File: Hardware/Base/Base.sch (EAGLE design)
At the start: 69 parts, among them T1 2N3904, T10 2N3904, T11 2N3904, T2 2N3904, T3 2N3904, T4 2N3904, T5 2N3904, T6 2N3904, T7 2N3904, T8 2N3904, T9 2N3904

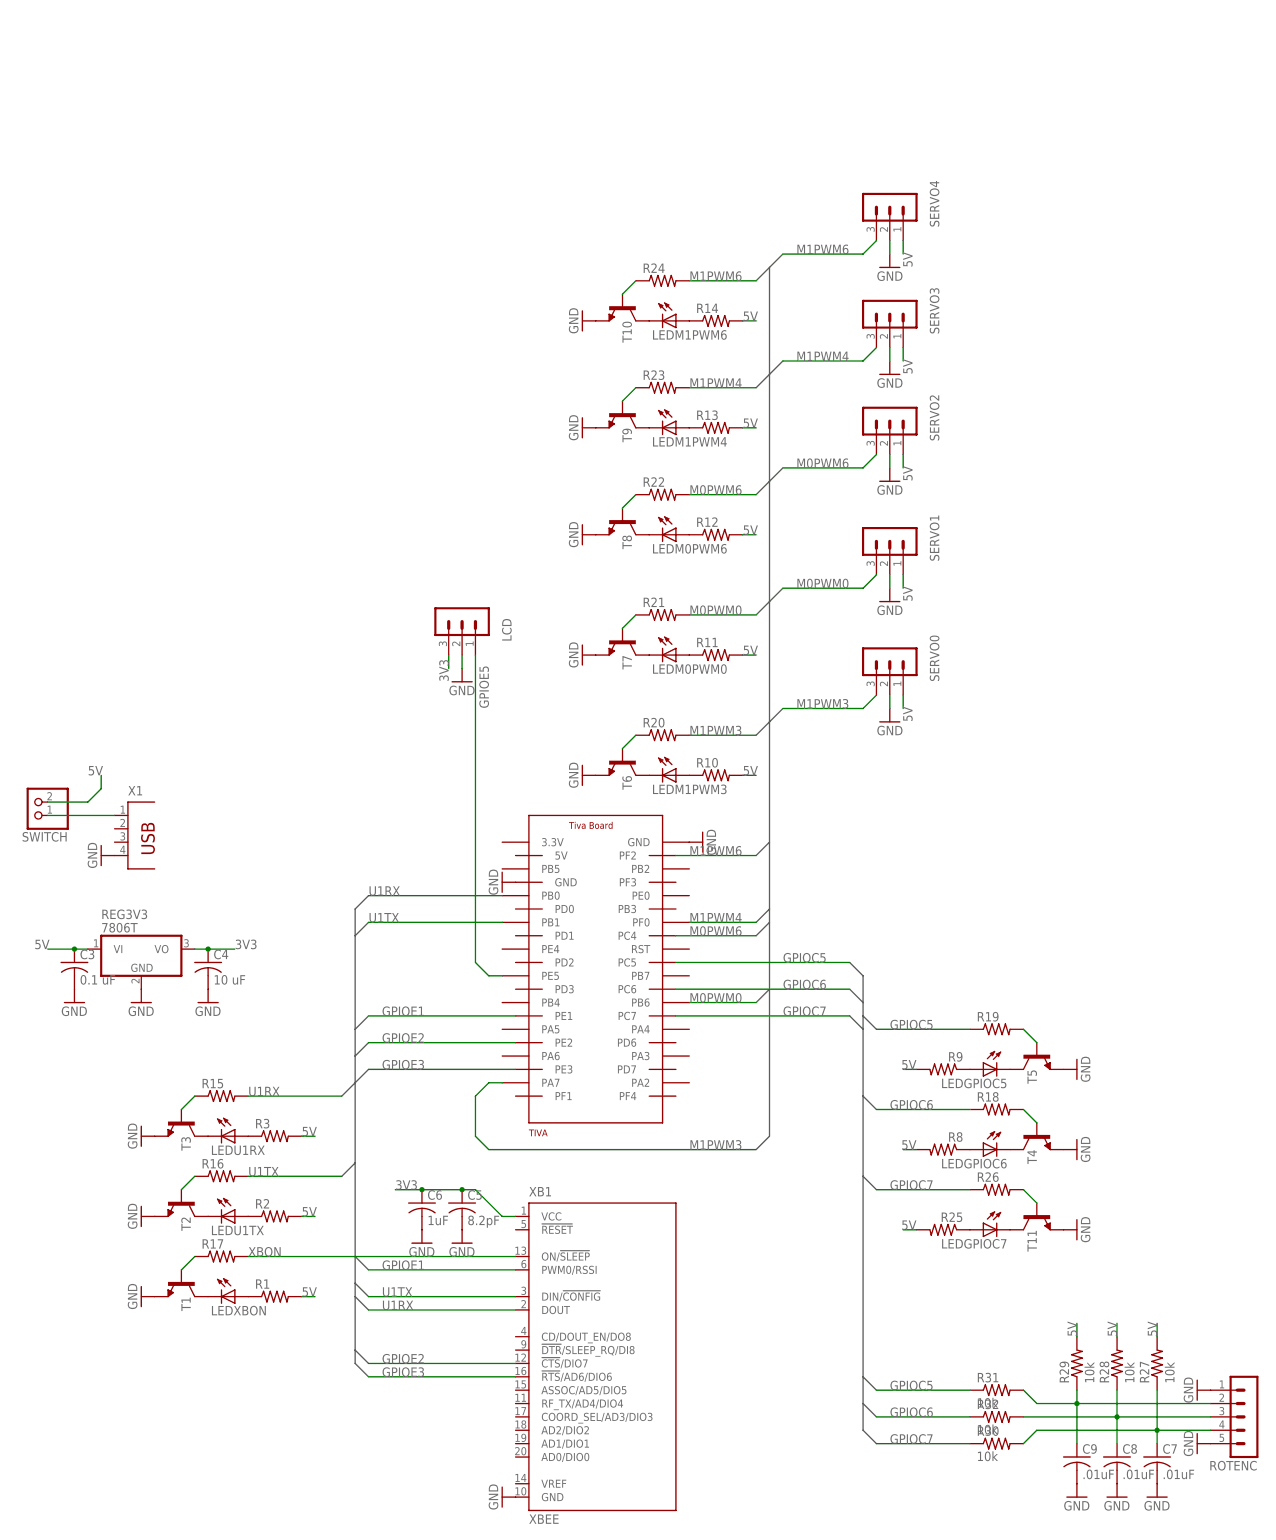
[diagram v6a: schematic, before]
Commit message: Initial layout of traces.
Updated power pins on Tiva Board device.
Added most traces (except Xbee connections and a few others).
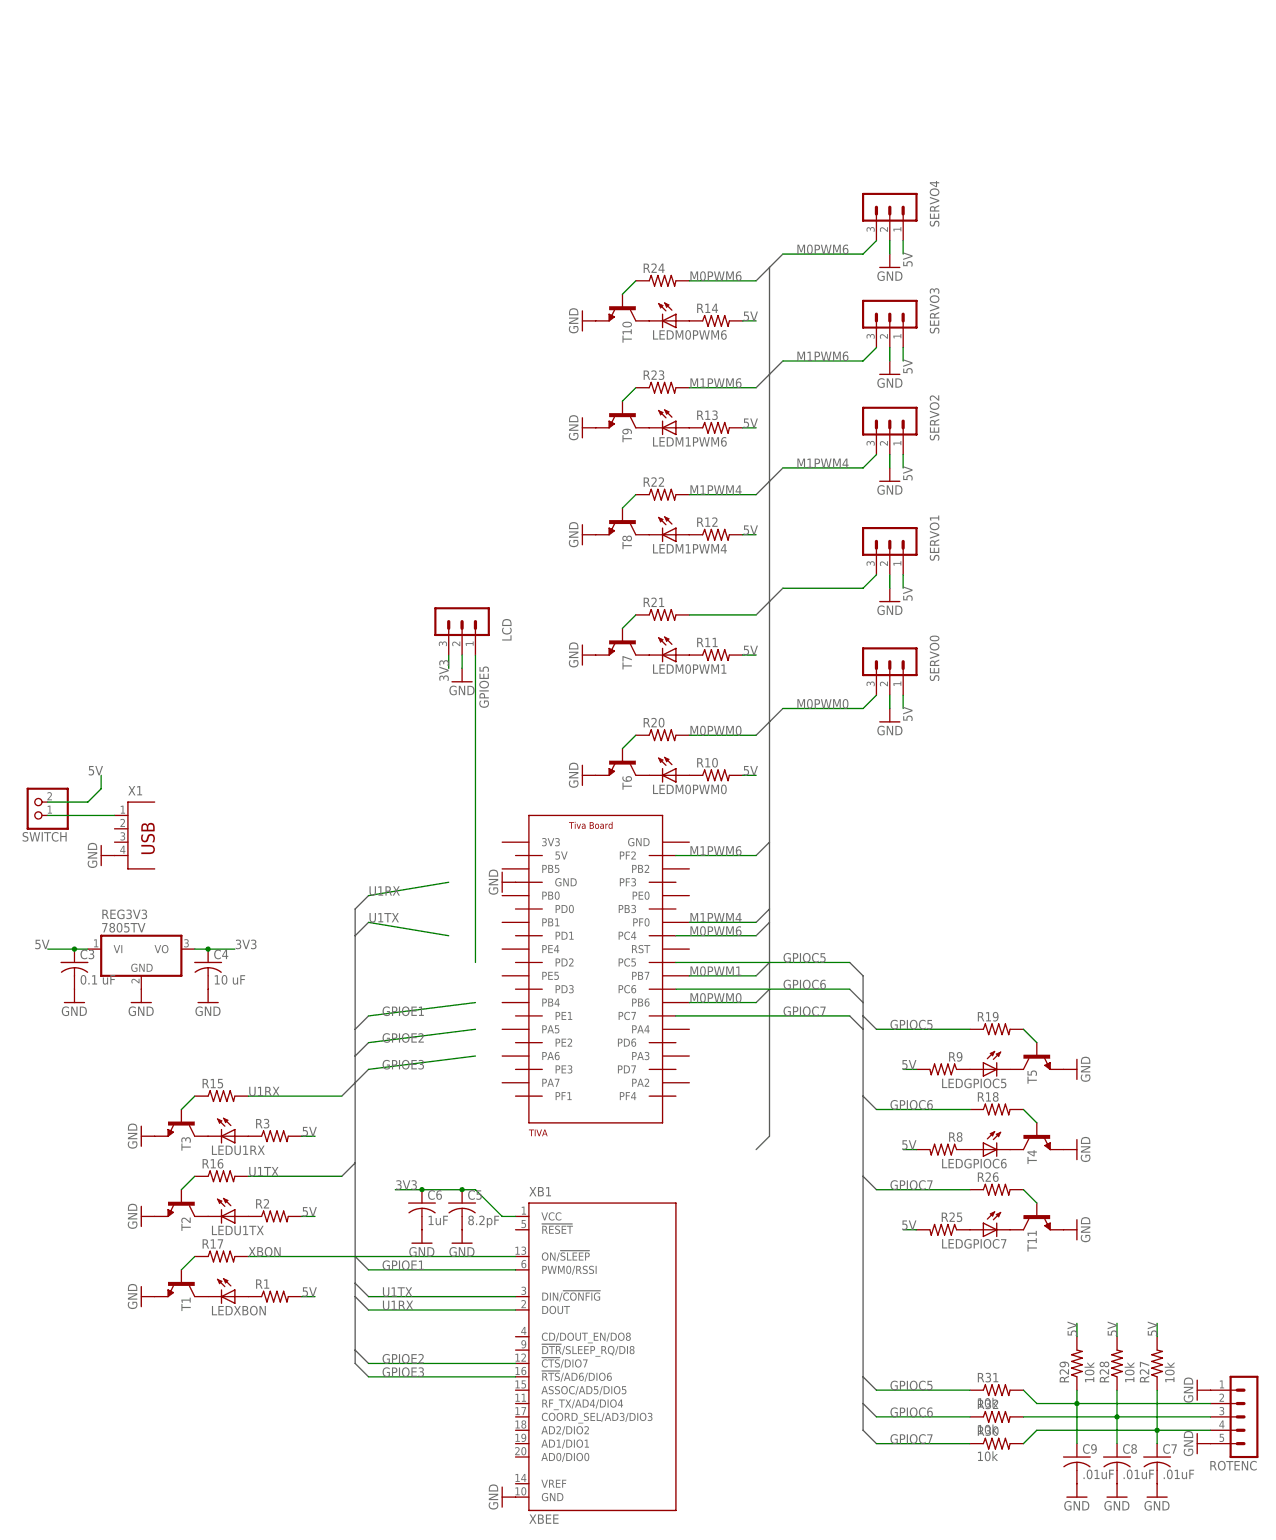
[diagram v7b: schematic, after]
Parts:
- removed LEDM1PWM3: (no value), led:LED5MM
- added LEDM0PWM1: (no value), led:LED5MM
- REG3V3: value 7806T -> 7805TV; device linear:7806T -> linear:7805TV
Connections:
- removed net M1PWM3: R20.2, SERVO0.3, TIVA.PA7
- new net M0PWM1: R21.2, SERVO1.3, TIVA.PB7
- net GND: no longer TIVA.GND@2
- net GPIOE1: no longer TIVA.PE1
- net GPIOE2: no longer TIVA.PE2
- net GPIOE3: no longer TIVA.PE3
- net GPIOE5: no longer TIVA.PE5
- net M0PWM0: now also R20.2, SERVO0.3; no longer R21.2, SERVO1.3
- net M0PWM6: now also R24.2, SERVO4.3; no longer R22.2, SERVO2.3
- net M1PWM4: now also R22.2, SERVO2.3; no longer R23.2, SERVO3.3
- net M1PWM6: now also R23.2, SERVO3.3; no longer R24.2, SERVO4.3
- net N$13: now also LEDM0PWM0.C; no longer LEDM1PWM3.C
- net N$14: now also LEDM0PWM0.A; no longer LEDM1PWM3.A
- net N$15: now also LEDM0PWM1.C; no longer LEDM0PWM0.C
- net N$16: now also LEDM0PWM1.A; no longer LEDM0PWM0.A
- net N$17: now also LEDM1PWM4.C; no longer LEDM0PWM6.C
- net N$18: now also LEDM1PWM4.A; no longer LEDM0PWM6.A
- net N$19: now also LEDM1PWM6.C; no longer LEDM1PWM4.C
- net N$20: now also LEDM1PWM6.A; no longer LEDM1PWM4.A
- net N$21: now also LEDM0PWM6.C; no longer LEDM1PWM6.C
- net N$22: now also LEDM0PWM6.A; no longer LEDM1PWM6.A
- net U1RX: no longer TIVA.PB0
- net U1TX: no longer TIVA.PB1
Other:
- moved on the sheet: LEDM0PWM0, LEDM0PWM6, LEDM1PWM4, LEDM1PWM6

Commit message: Add level shifter.
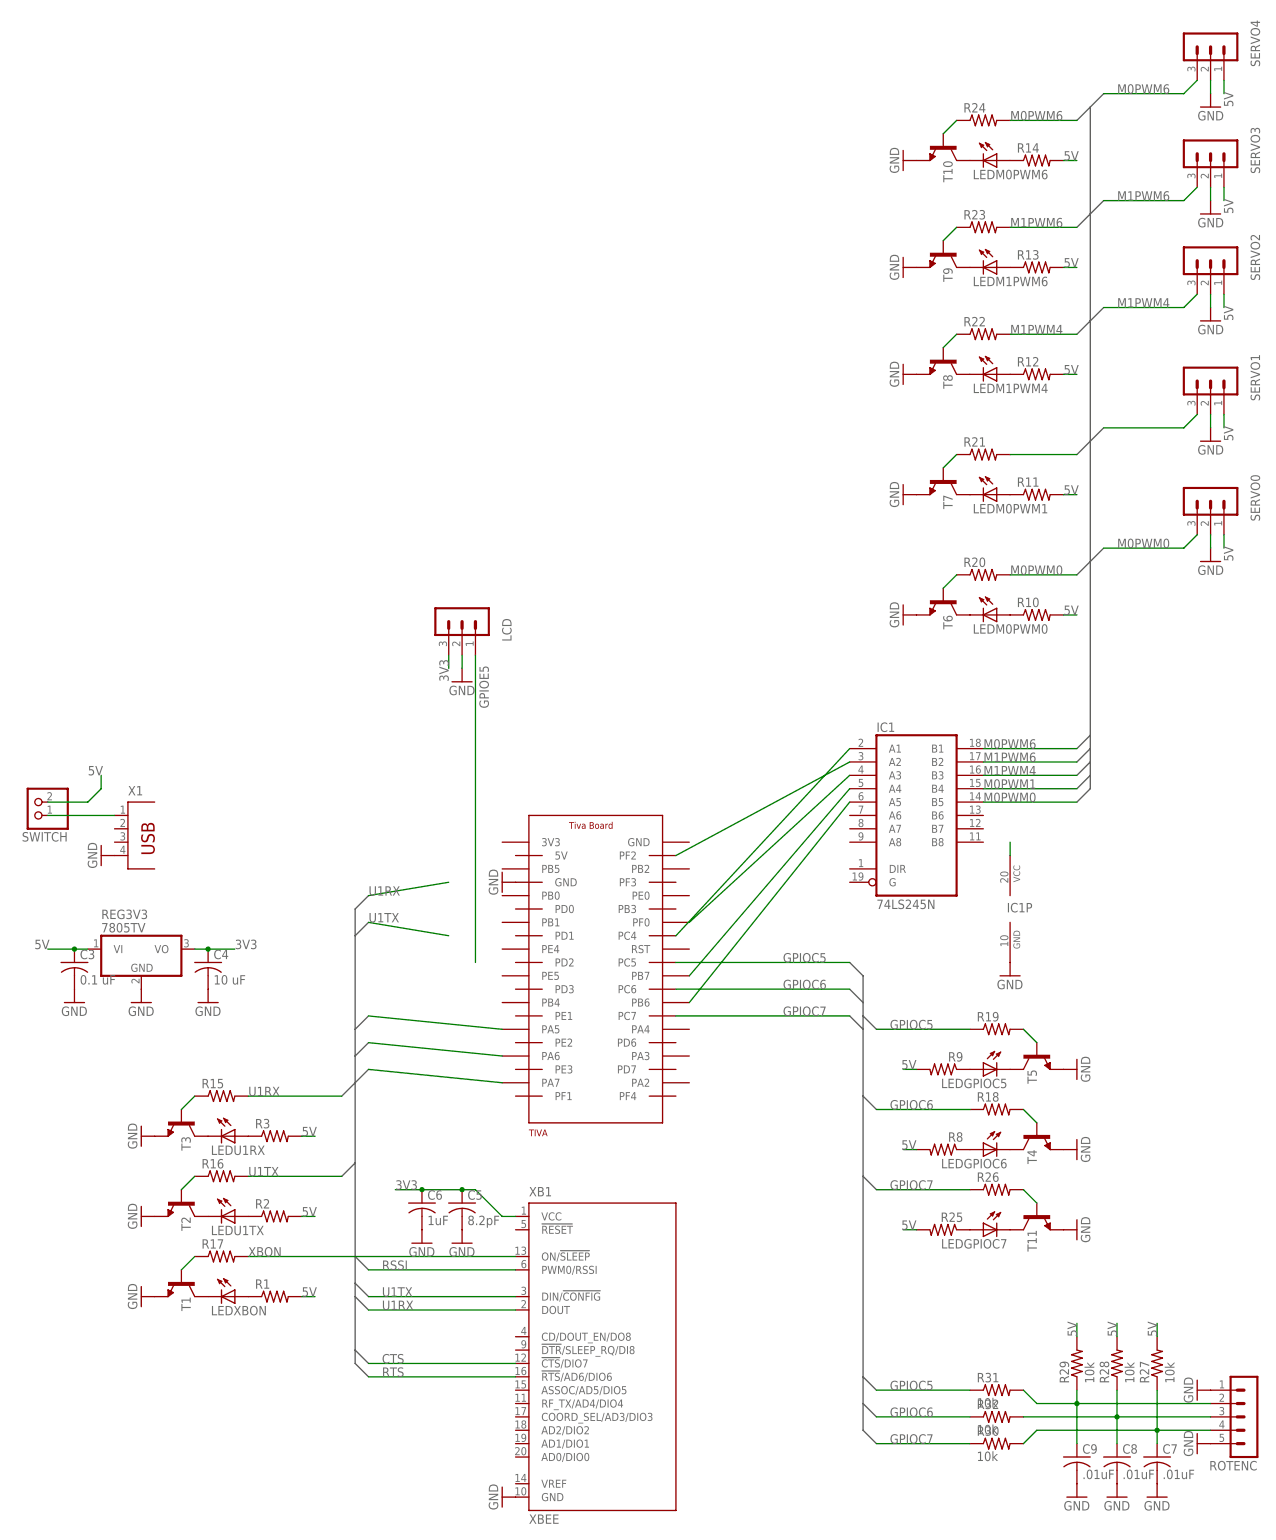
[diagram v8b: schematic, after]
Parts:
- added IC1: 74LS245N, 74xx-us:74LS245N
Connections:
- removed net GPIOE1: XB1.PWM0/RSSI
- removed net GPIOE2: XB1.!CTS!/DIO7
- removed net GPIOE3: XB1.!RTS!/AD6/DIO6
- new net CTS: TIVA.PA5, XB1.!CTS!/DIO7
- new net N$39: IC1A.A3, TIVA.PF0
- new net N$40: IC1A.A2, TIVA.PF2
- new net N$41: IC1A.A4, TIVA.PB7
- new net N$42: IC1A.A5, TIVA.PB6
- new net N$8: IC1A.A1, TIVA.PC4
- new net RSSI: TIVA.PA7, XB1.PWM0/RSSI
- new net RTS: TIVA.PA6, XB1.!RTS!/AD6/DIO6
- net 5V: now also IC1P.VCC
- net GND: now also IC1P.GND
- net M0PWM0: now also IC1A.B5; no longer TIVA.PB6
- net M0PWM1: now also IC1A.B4; no longer TIVA.PB7
- net M0PWM6: now also IC1A.B1; no longer TIVA.PC4
- net M1PWM4: now also IC1A.B3; no longer TIVA.PF0
- net M1PWM6: now also IC1A.B2; no longer TIVA.PF2
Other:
- moved on the sheet: LEDM0PWM0, LEDM0PWM1, LEDM0PWM6, LEDM1PWM4, LEDM1PWM6, R10, R11, R12, R13, R14, R20, R21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
